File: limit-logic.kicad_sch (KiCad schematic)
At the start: 10 parts, among them U17001 4043, U17002 4043, U17003 4078, U17004 4081, U17005 4073, U17006 4071, U17007 4069

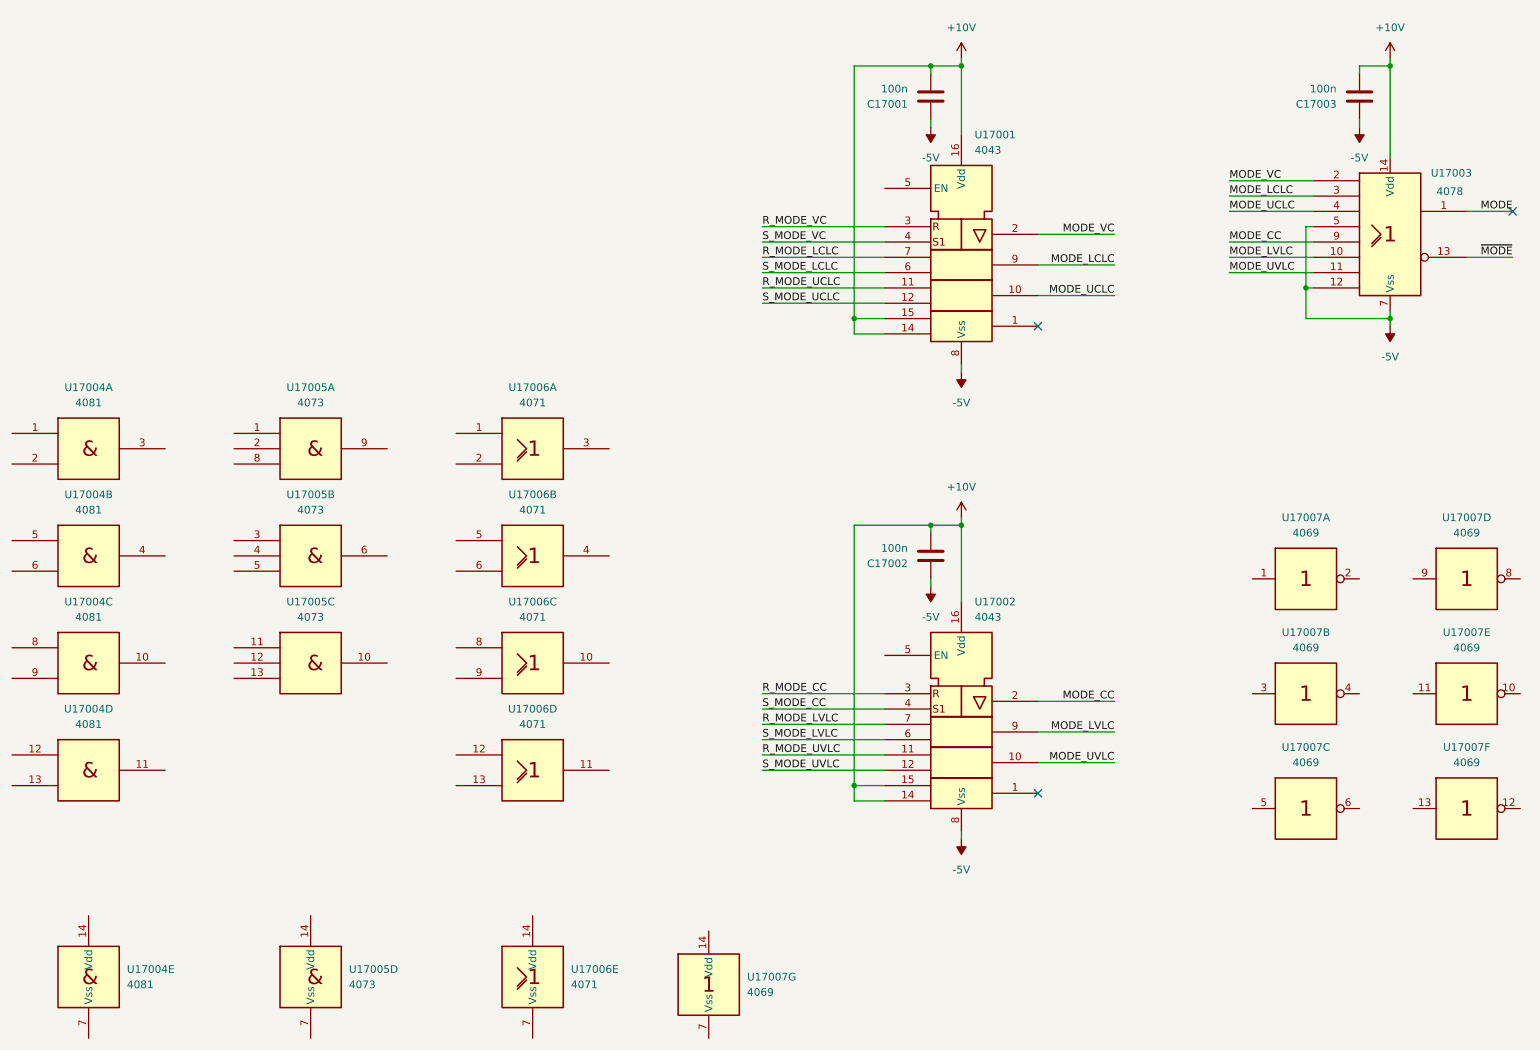
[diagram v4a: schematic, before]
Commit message: refactor schematic hirarchy
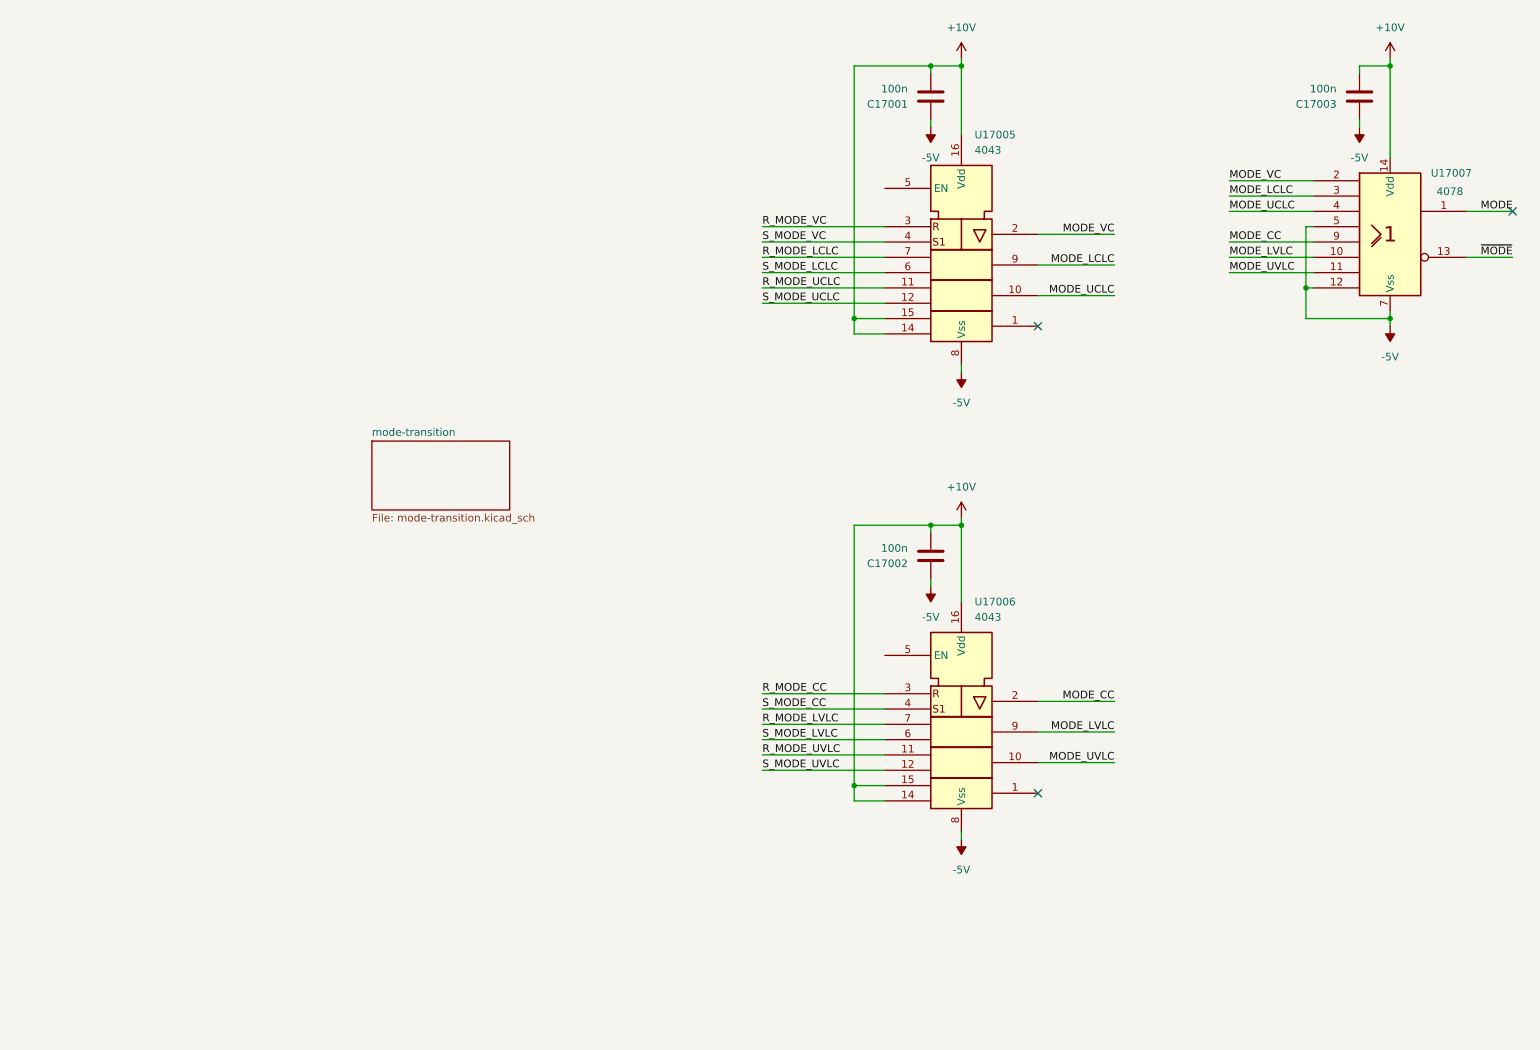
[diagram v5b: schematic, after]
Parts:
- removed U17004: 4081, Package_SO:SOIC-14_3.9x8.7mm_P1.27mm, symbol pss:4081
- removed U17005: 4073, Package_SO:SOIC-14_3.9x8.7mm_P1.27mm, symbol pss:4073
- removed U17006: 4071, Package_SO:SOIC-14_3.9x8.7mm_P1.27mm, symbol pss:4071
- removed U17007: 4069, Package_SO:SOIC-14_3.9x8.7mm_P1.27mm, symbol pss:4069
- renumbered U17001 to U17005, U17002 to U17006, U17003 to U17007
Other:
- added sheet mode-transition (mode-transition.kicad_sch)

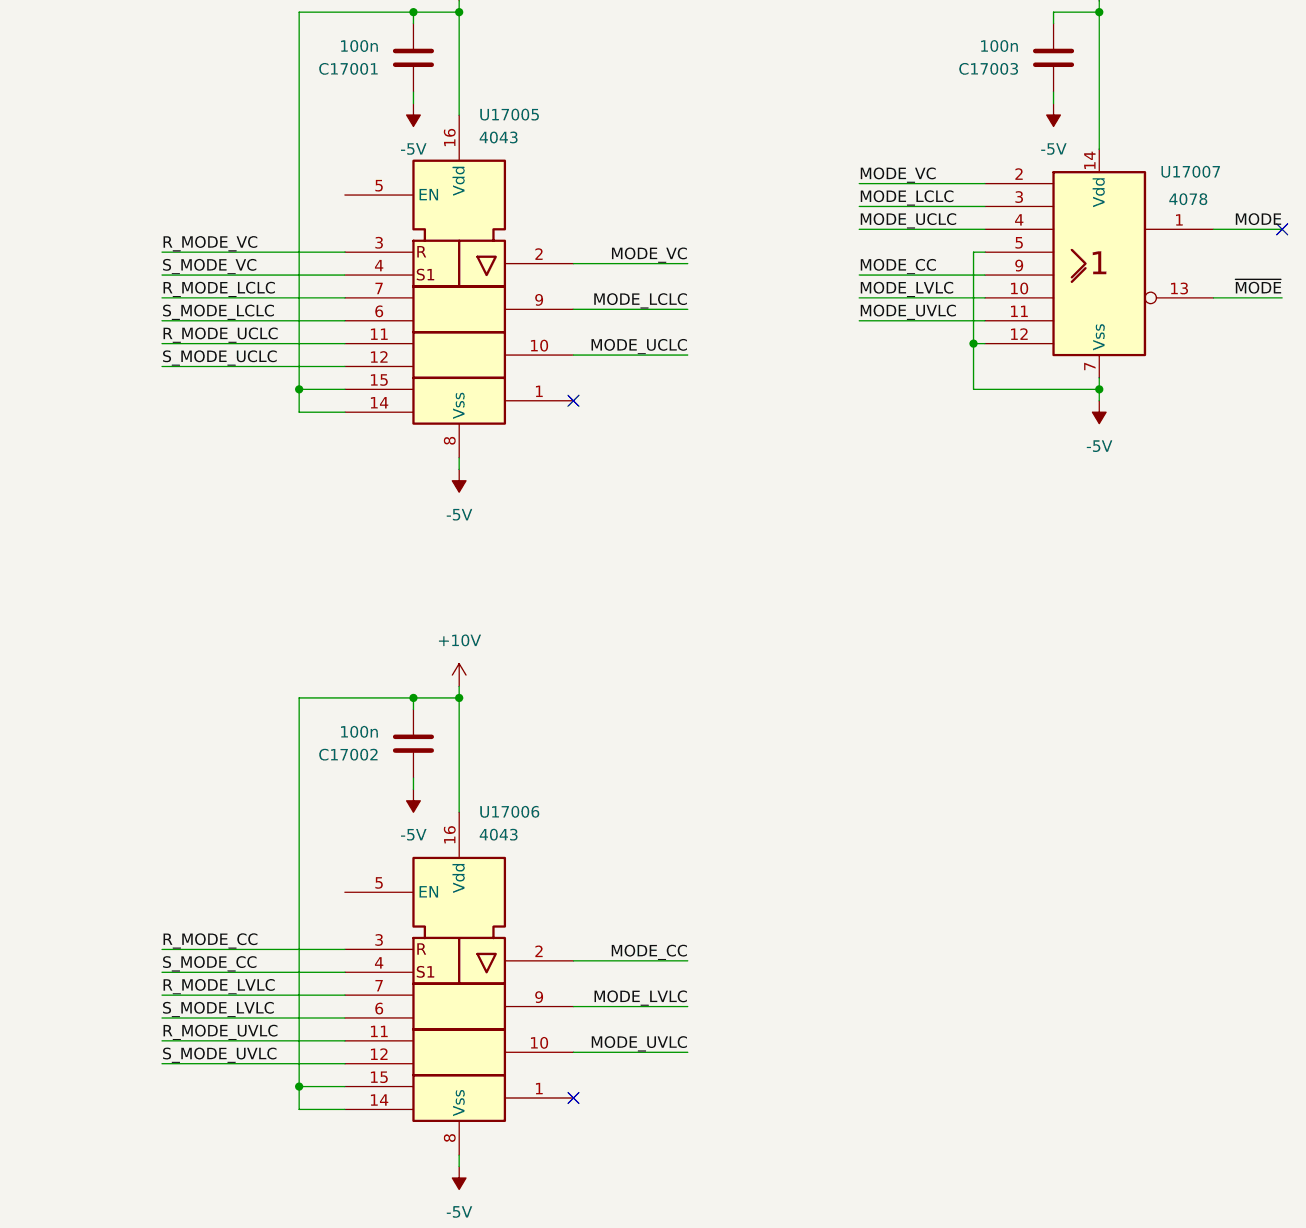
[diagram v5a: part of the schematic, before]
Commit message: add limit-logic mode transition logic
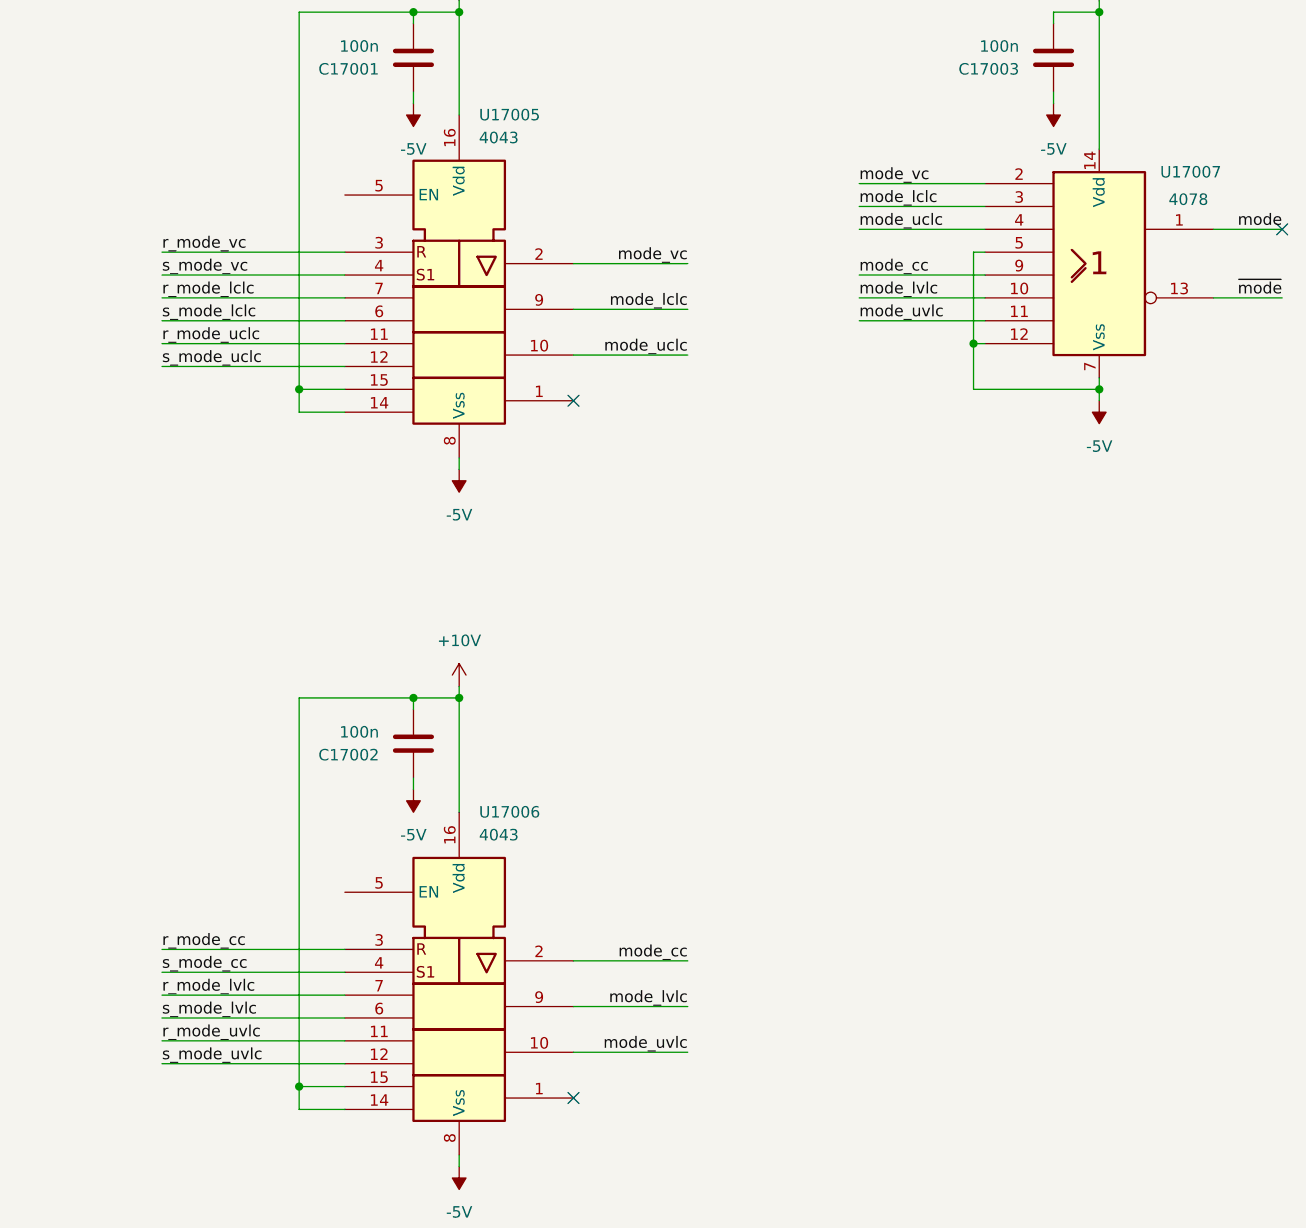
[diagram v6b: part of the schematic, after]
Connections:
- net MODE renamed mode
- net MODE_CC renamed mode_cc
- net MODE_LCLC renamed mode_lclc
- net MODE_LVLC renamed mode_lvlc
- net MODE_UCLC renamed mode_uclc
- net MODE_UVLC renamed mode_uvlc
- net MODE_VC renamed mode_vc
- net R_MODE_CC renamed r_mode_cc
- net R_MODE_LCLC renamed r_mode_lclc
- net R_MODE_LVLC renamed r_mode_lvlc
- net R_MODE_UCLC renamed r_mode_uclc
- net R_MODE_UVLC renamed r_mode_uvlc
- net R_MODE_VC renamed r_mode_vc
- net S_MODE_CC renamed s_mode_cc
- net S_MODE_LCLC renamed s_mode_lclc
- net S_MODE_LVLC renamed s_mode_lvlc
- net S_MODE_UCLC renamed s_mode_uclc
- net S_MODE_UVLC renamed s_mode_uvlc
- net S_MODE_VC renamed s_mode_vc
- net ~{MODE} renamed ~{mode}
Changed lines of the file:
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@@
 		)
 	)
-	(label "MODE_LVLC"
+	(label "mode_lvlc"
 		(at 203.2 137.16 180)
 		(fields_autoplaced yes)
@@
 		)
 	)
-	(label "MODE_LCLC"
+	(label "mode_lclc"
 		(at 203.2 59.69 180)
 		(fields_autoplaced yes)
@@
 		)
 	)
-	(label "R_MODE_CC"
+	(label "r_mode_cc"
 		(at 144.78 130.81 0)
 		(fields_autoplaced yes)
@@
 		)
 	)
-	(label "MODE"
+	(label "mode"
 		(at 269.24 50.8 180)
 		(fields_autoplaced yes)
@@
 		)
 	)
-	(label "MODE_UCLC"
+	(label "mode_uclc"
 		(at 203.2 64.77 180)
 		(fields_autoplaced yes)
@@
 		)
 	)
-	(label "MODE_VC"
+	(label "mode_vc"
 		(at 203.2 54.61 180)
 		(fields_autoplaced yes)
@@
 		)
 	)
-	(label "R_MODE_LCLC"
+	(label "r_mode_lclc"
 		(at 144.78 58.42 0)
 		(fields_autoplaced yes)
@@
 		)
 	)
-	(label "S_MODE_UCLC"
+	(label "s_mode_uclc"
 		(at 144.78 66.04 0)
 		(fields_autoplaced yes)
@@
 		)
 	)
-	(label "R_MODE_VC"
+	(label "r_mode_vc"
 		(at 144.78 53.34 0)
 		(fields_autoplaced yes)
@@
 		)
 	)
-	(label "R_MODE_UCLC"
+	(label "r_mode_uclc"
 		(at 144.78 63.5 0)
 		(fields_autoplaced yes)
@@
 		)
 	)
-	(label "S_MODE_LVLC"
+	(label "s_mode_lvlc"
 		(at 144.78 138.43 0)
 		(fields_autoplaced yes)
@@
 		)
 	)
-	(label "MODE_UVLC"
+	(label "mode_uvlc"
 		(at 222.25 60.96 0)
 		(fields_autoplaced yes)
@@
 		)
 	)
-	(label "S_MODE_LCLC"
+	(label "s_mode_lclc"
 		(at 144.78 60.96 0)
 		(fields_autoplaced yes)
@@
 		)
 	)
-	(label "MODE_UCLC"
+	(label "mode_uclc"
 		(at 222.25 50.8 0)
 		(fields_autoplaced yes)
@@
 		)
 	)
-	(label "~{MODE}"
+	(label "~{mode}"
 		(at 269.24 58.42 180)
 		(fields_autoplaced yes)
@@
 		)
 	)
-	(label "MODE_LCLC"
+	(label "mode_lclc"
 		(at 222.25 48.26 0)
 		(fields_autoplaced yes)
@@
 		)
 	)
-	(label "MODE_UVLC"
+	(label "mode_uvlc"
 		(at 203.2 142.24 180)
 		(fields_autoplaced yes)
@@
 		)
 	)
-	(label "MODE_LVLC"
+	(label "mode_lvlc"
 		(at 222.25 58.42 0)
 		(fields_autoplaced yes)
@@
 		)
 	)
-	(label "MODE_CC"
+	(label "mode_cc"
 		(at 203.2 132.08 180)
 		(fields_autoplaced yes)
@@
 		)
 	)
-	(label "R_MODE_LVLC"
+	(label "r_mode_lvlc"
 		(at 144.78 135.89 0)
 		(fields_autoplaced yes)
@@
 		)
 	)
-	(label "S_MODE_VC"
+	(label "s_mode_vc"
 		(at 144.78 55.88 0)
 		(fields_autoplaced yes)
@@
 		)
 	)
-	(label "S_MODE_CC"
+	(label "s_mode_cc"
 		(at 144.78 133.35 0)
 		(fields_autoplaced yes)
@@
 		)
 	)
-	(label "S_MODE_UVLC"
+	(label "s_mode_uvlc"
 		(at 144.78 143.51 0)
 		(fields_autoplaced yes)
@@
 		)
 	)
-	(label "R_MODE_UVLC"
+	(label "r_mode_uvlc"
 		(at 144.78 140.97 0)
 		(fields_autoplaced yes)
@@
 		)
 	)
-	(label "MODE_CC"
+	(label "mode_cc"
 		(at 222.25 55.88 0)
 		(fields_autoplaced yes)
@@
 		)
 	)
-	(label "MODE_VC"
+	(label "mode_vc"
 		(at 222.25 45.72 0)
 		(fields_autoplaced yes)
